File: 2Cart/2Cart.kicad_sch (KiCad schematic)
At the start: 11 parts, among them J1 CommanderX16Expansion Alt, U1 SST39SF040, U2 74HCT00, U3 74HCT138, U4 AS6C4008-55PCN

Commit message: Flip the board
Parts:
- C1, C2, C3, C4: value C -> 100nF
- U1: value SST39SF040 -> SST39SF040 (ROM)
- U4: value AS6C4008-55PCN -> AS6C4008 (RAM)
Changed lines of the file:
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@@
 			)
 		)
-		(property "Value" "AS6C4008-55PCN"
+		(property "Value" "AS6C4008 (RAM)"
 			(at 74.5841 34.29 0)
 			(effects
@@
 			)
 		)
-		(property "Value" "C"
+		(property "Value" "100nF"
 			(at 68.58 109.22 90)
 			(effects
@@
 			)
 		)
-		(property "Value" "C"
+		(property "Value" "100nF"
 			(at 67.31 25.4 90)
 			(effects
@@
 			)
 		)
-		(property "Value" "SST39SF040"
+		(property "Value" "SST39SF040 (ROM)"
 			(at 75.8541 120.65 0)
 			(effects
@@
 			)
 		)
-		(property "Value" "C"
+		(property "Value" "100nF"
 			(at 222.25 21.59 90)
 			(effects
@@
 		(dnp no)
 		(property "Reference" "U2"
-			(at 238.506 136.652 0)
+			(at 244.602 139.446 90)
 			(effects
 				(font
@@
 		)
 		(property "Value" "74HCT00"
-			(at 241.046 136.652 0)
+			(at 244.602 136.906 90)
 			(effects
 				(font
@@
 			)
 		)
-		(property "Value" "C"
+		(property "Value" "100nF"
 			(at 229.87 152.3999 0)
 			(effects

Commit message: Polish and a readme explaining WTF
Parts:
- C1, C2, C3, C4: footprint Capacitor_THT:C_Disc_D5.0mm_W2.5mm_P5.00mm -> Capacitor_THT:C_Axial_L3.8mm_D2.6mm_P7.50mm_Horizontal
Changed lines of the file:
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@@
 			)
 		)
-		(property "Footprint" "Capacitor_THT:C_Disc_D5.0mm_W2.5mm_P5.00mm"
+		(property "Footprint" "Capacitor_THT:C_Axial_L3.8mm_D2.6mm_P7.50mm_Horizontal"
 			(at 72.39 113.3348 0)
 			(effects
@@
 			)
 		)
-		(property "Footprint" "Capacitor_THT:C_Disc_D5.0mm_W2.5mm_P5.00mm"
+		(property "Footprint" "Capacitor_THT:C_Axial_L3.8mm_D2.6mm_P7.50mm_Horizontal"
 			(at 71.12 29.5148 0)
 			(effects
@@
 			)
 		)
-		(property "Footprint" "Capacitor_THT:C_Disc_D5.0mm_W2.5mm_P5.00mm"
+		(property "Footprint" "Capacitor_THT:C_Axial_L3.8mm_D2.6mm_P7.50mm_Horizontal"
 			(at 218.44 27.6352 0)
 			(effects
@@
 			)
 		)
-		(property "Footprint" "Capacitor_THT:C_Disc_D5.0mm_W2.5mm_P5.00mm"
+		(property "Footprint" "Capacitor_THT:C_Axial_L3.8mm_D2.6mm_P7.50mm_Horizontal"
 			(at 225.0948 147.32 0)
 			(effects

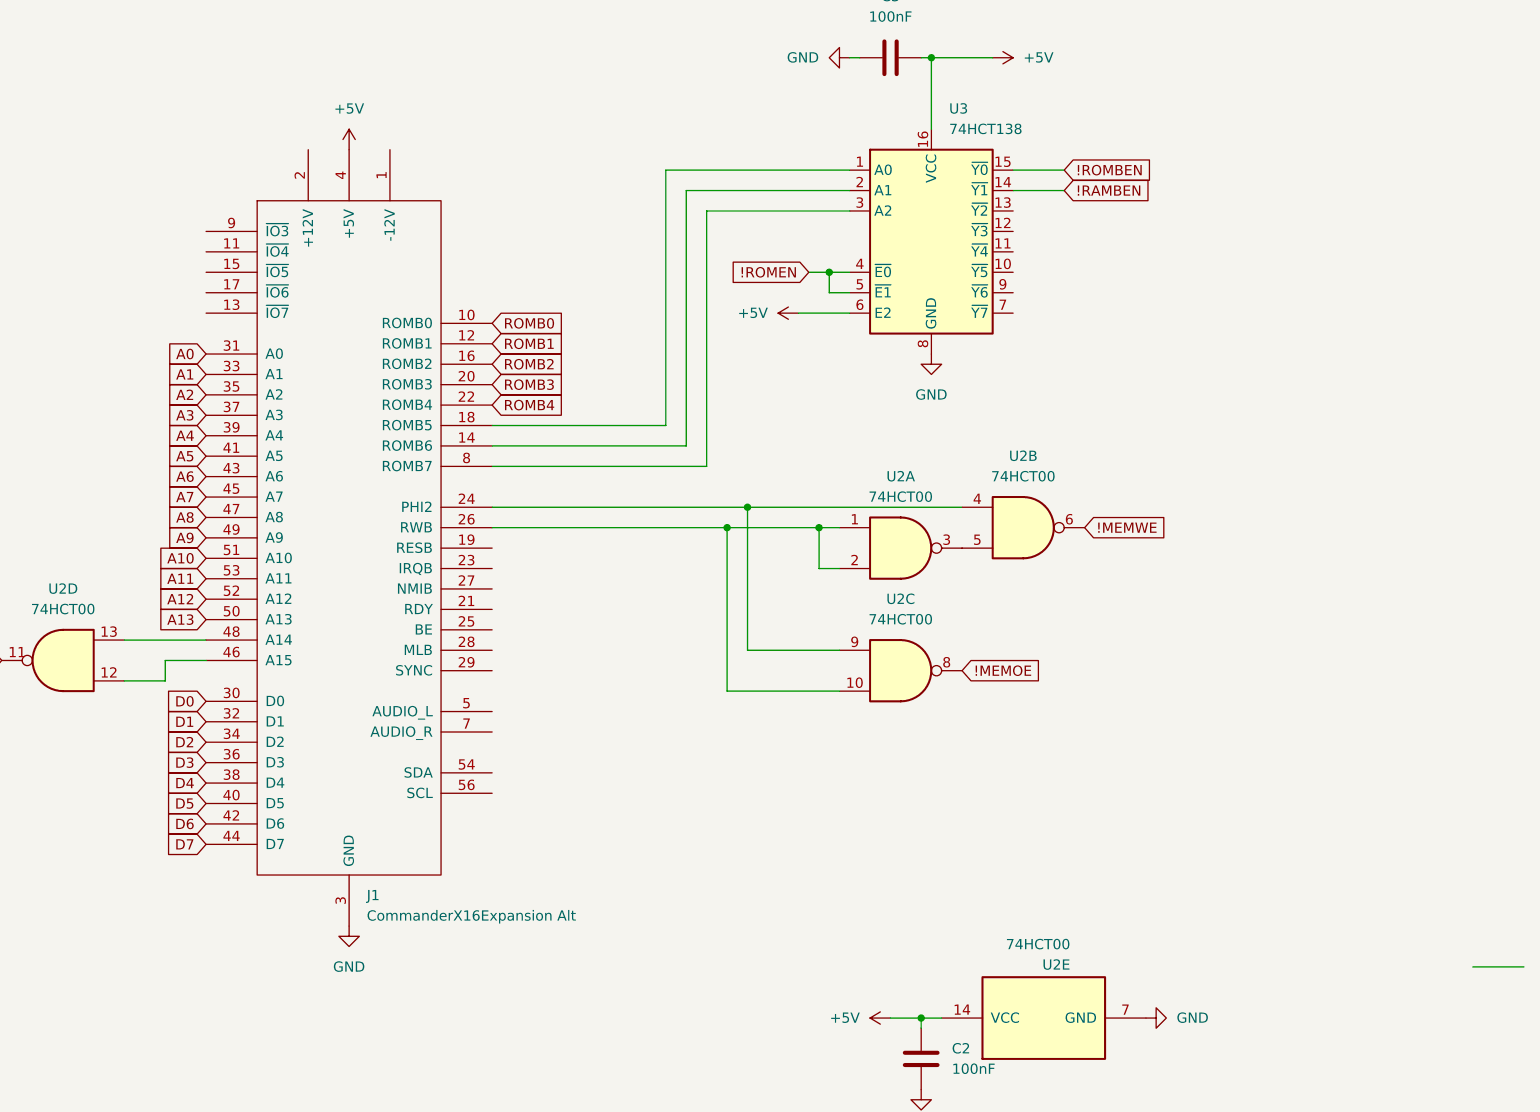
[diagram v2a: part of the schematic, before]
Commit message: Two layer routing with copper pours
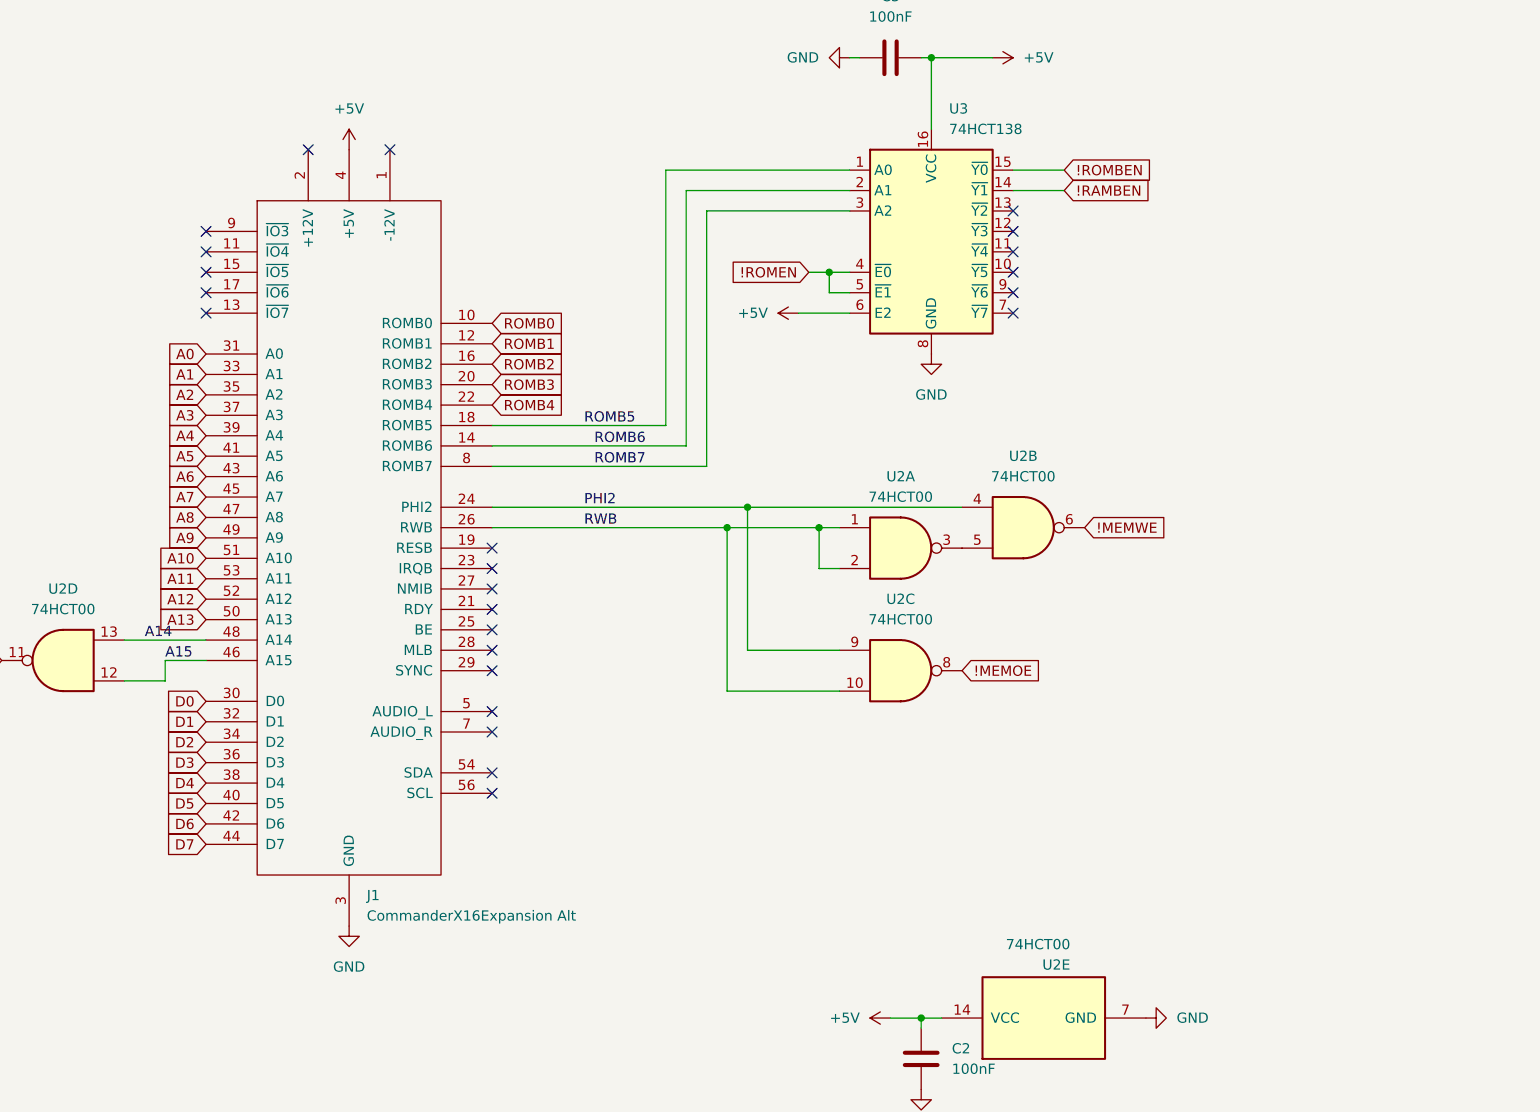
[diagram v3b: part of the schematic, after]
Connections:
- net ROMB5: now reaches J1.18 (ROMB5), U3.1 (A0)
- net ROMB6: now reaches J1.14 (ROMB6), U3.2 (A1)
- net ROMB7: now reaches J1.8 (ROMB7), U3.3 (A2)
- net RWB: now reaches J1.26 (RWB), U2.1, U2.10, U2.2
- net PHI2: now reaches J1.24 (PHI2), U2.4, U2.9
- net A15: now reaches J1.46 (A15), U2.12
- net A14: now reaches J1.48 (A14), U2.13
- no-connect marks 0 -> 24
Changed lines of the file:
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@@
 		(color 0 0 0 0)
 	)
+	(no_connect
+		(at 137.16 55.88)
+	)
+	(no_connect
+		(at 237.49 55.88)
+	)
+	(no_connect
+		(at 172.72 87.63)
+	)
+	(no_connect
+		(at 237.49 50.8)
+	)
+	(no_connect
+		(at 137.16 48.26)
+	)
+	(no_connect
+		(at 137.16 53.34)
+	)
+	(no_connect
+		(at 149.86 38.1)
+	)
+	(no_connect
+		(at 237.49 48.26)
+	)
+	(no_connect
+		(at 172.72 100.33)
+	)
+	(no_connect
+		(at 172.72 97.79)
+	)
+	(no_connect
+		(at 237.49 58.42)
+	)
+	(no_connect
+		(at 172.72 110.49)
+	)
+	(no_connect
+		(at 172.72 102.87)
+	)
+	(no_connect
+		(at 137.16 58.42)
+	)
+	(no_connect
+		(at 172.72 115.57)
+	)
+	(no_connect
+		(at 172.72 118.11)
+	)
+	(no_connect
+		(at 172.72 107.95)
+	)
+	(no_connect
+		(at 237.49 45.72)
+	)
+	(no_connect
+		(at 160.02 38.1)
+	)
+	(no_connect
+		(at 172.72 90.17)
+	)
+	(no_connect
+		(at 172.72 92.71)
+	)
+	(no_connect
+		(at 172.72 95.25)
+	)
+	(no_connect
+		(at 137.16 50.8)
+	)
+	(no_connect
+		(at 237.49 53.34)
+	)
 	(wire
 		(pts
@@
 	(wire
 		(pts
-			(xy 294.64 139.7) (xy 300.99 139.7)
-		)
-		(stroke
-			(width 0)
-			(type default)
-		)
-	)
-	(wire
-		(pts
 			(xy 217.17 26.67) (xy 218.44 26.67)
 		)
@@
 		)
 	)
+	(label "ROMB5"
+		(at 184.15 72.39 0)
+		(fields_autoplaced yes)
+		(effects
+			(font
+				(size 1.27 1.27)
+			)
+			(justify left bottom)
+		)
+	)
+	(label "A15"
+		(at 132.08 101.6 0)
+		(fields_autoplaced yes)
+		(effects
+			(font
+				(size 1.27 1.27)
+			)
+			(justify left bottom)
+		)
+	)
+	(label "ROMB7"
+		(at 185.42 77.47 0)
+		(fields_autoplaced yes)
+		(effects
+			(font
+				(size 1.27 1.27)
+			)
+			(justify left bottom)
+		)
+	)
+	(label "A14"
+		(at 129.54 99.06 0)
+		(fields_autoplaced yes)
+		(effects
+			(font
+				(size 1.27 1.27)
+			)
+			(justify left bottom)
+		)
+	)
+	(label "ROMB6"
+		(at 185.42 74.93 0)
+		(fields_autoplaced yes)
+		(effects
+			(font
+				(size 1.27 1.27)
+			)
+			(justify left bottom)
+		)
+	)
+	(label "PHI2"
+		(at 184.15 82.55 0)
+		(fields_autoplaced yes)
+		(effects
+			(font
+				(size 1.27 1.27)
+			)
+			(justify left bottom)
+		)
+	)
+	(label "RWB"
+		(at 184.15 85.09 0)
+		(fields_autoplaced yes)
+		(effects
+			(font
+				(size 1.27 1.27)
+			)
+			(justify left bottom)
+		)
+	)

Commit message: Added I2C NVRAM
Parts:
- added C5: 100nF, Capacitor_THT:C_Axial_L3.8mm_D2.6mm_P7.50mm_Horizontal, symbol Device:C_Small
- added R2, R3: 100K, Resistor_THT:R_Axial_DIN0204_L3.6mm_D1.6mm_P5.08mm_Horizontal, symbol Device:R_Small
- added SW1: SW_DIP_x04, Button_Switch_THT:SW_DIP_SPSTx04_Slide_9.78x12.34mm_W7.62mm_P2.54mm, symbol Switch:SW_DIP_x04
- added U5: FM24C64B, Package_SO:SOIC-8_3.9x4.9mm_P1.27mm, symbol Memory_NVRAM:FM24C64B
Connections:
- net +5V: now also C5.2, R2.2, R3.1, U5.8 (VDD)
- net GND: now also C5.1, SW1.4, U5.4 (VSS)
- net SDA: now reaches J1.54 (SDA)
- net SDA: now also U5.5 (SDA)
- net SCL: now reaches J1.56 (SCL)
- net SCL: now also U5.6 (SCL)
- new net: R3.2, SW1.1, SW1.2, SW1.3
- new net FA0: SW1.8, U5.1 (A0)
- new net FA1: SW1.7, U5.2 (A1)
- new net FA2: SW1.6, U5.3 (A2)
- new net WP: R2.1, SW1.5, U5.7 (WP)
- no-connect marks 24 -> 22
